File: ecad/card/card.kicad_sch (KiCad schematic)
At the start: 136 parts, among them J1 Conn_01x03_Pin, J2 USB4105-GF-A, J3 10145226-0241N13LF, J4 Conn_01x03_Pin, J5 Conn_01x03_Pin, SW1 SW_Push, SW2 SW_Push, U1 W25Q128JVS, U2 RP2350_80QFN, U3 MCP23017_SO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

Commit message: new panel routing
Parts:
- SW1, SW2: value SW_Push -> TS-1187A-B-A-B
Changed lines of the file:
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@@
 			)
 		)
-		(property "Value" "SW_Push"
+		(property "Value" "TS-1187A-B-A-B"
 			(at 30.48 94.742 0)
 			(effects
@@
 			)
 		)
-		(property "Value" "SW_Push"
+		(property "Value" "TS-1187A-B-A-B"
 			(at 32.512 205.74 0)
 			(effects

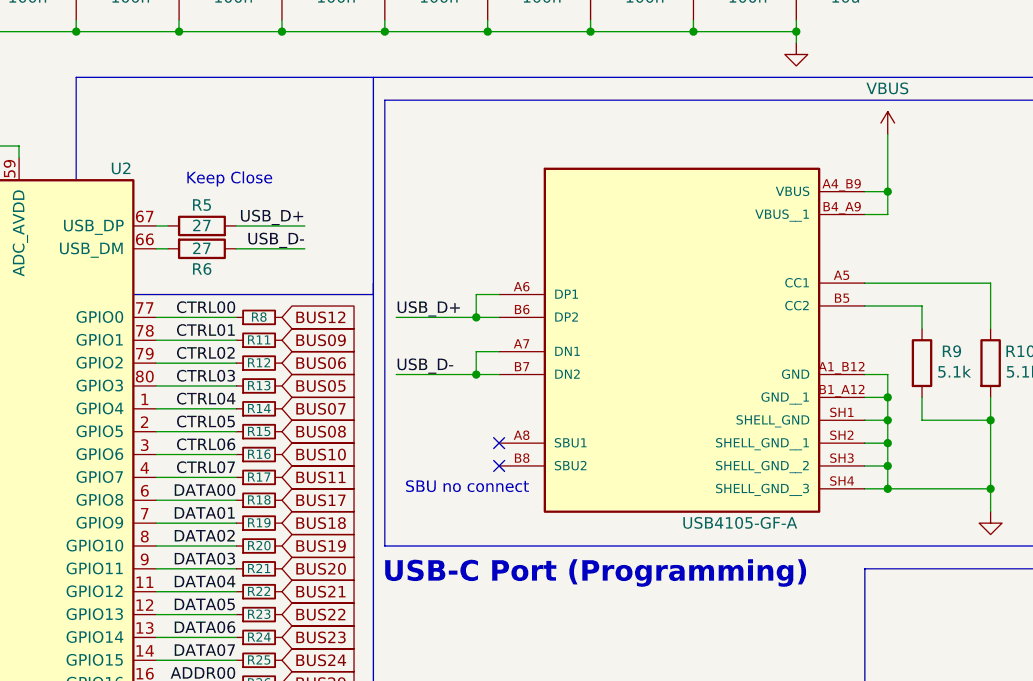
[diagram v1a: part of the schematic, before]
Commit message: stackup changes, prodction
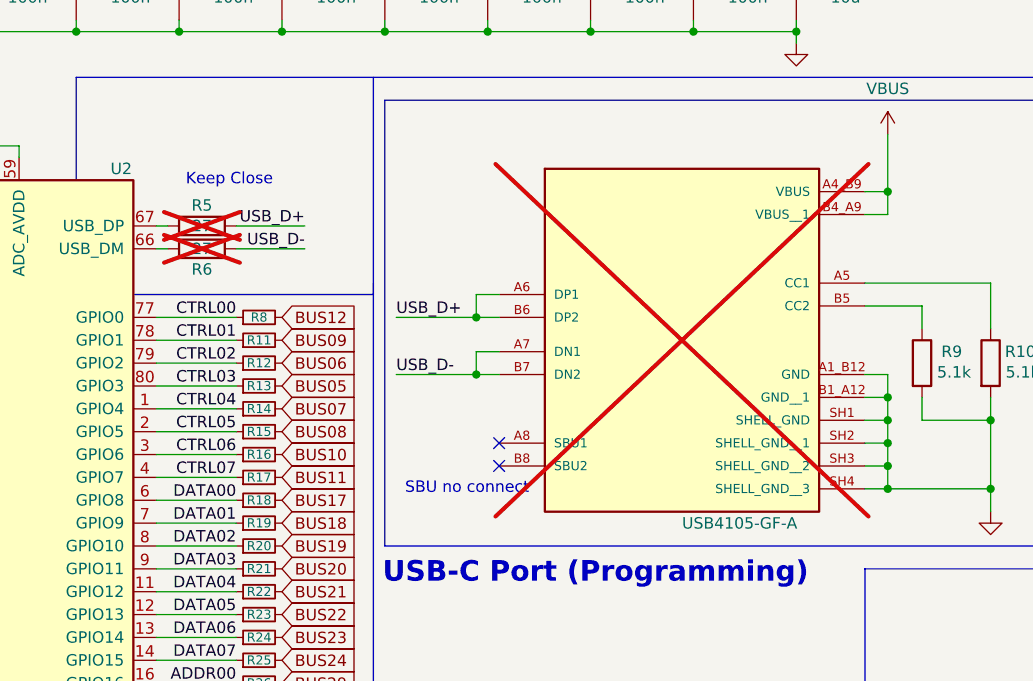
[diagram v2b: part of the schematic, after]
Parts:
- J2, R5, R6: now not fitted
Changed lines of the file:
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@@
 		(in_bom yes)
 		(on_board yes)
-		(dnp no)
+		(dnp yes)
 		(property "Reference" "J2"
 			(at 291.846 38.862 0)
@@
 		(in_bom yes)
 		(on_board yes)
-		(dnp no)
+		(dnp yes)
 		(property "Reference" "R6"
 			(at 146.05 64.516 90)
@@
 		(in_bom yes)
 		(on_board yes)
-		(dnp no)
+		(dnp yes)
 		(property "Reference" "R5"
 			(at 146.05 57.404 90)

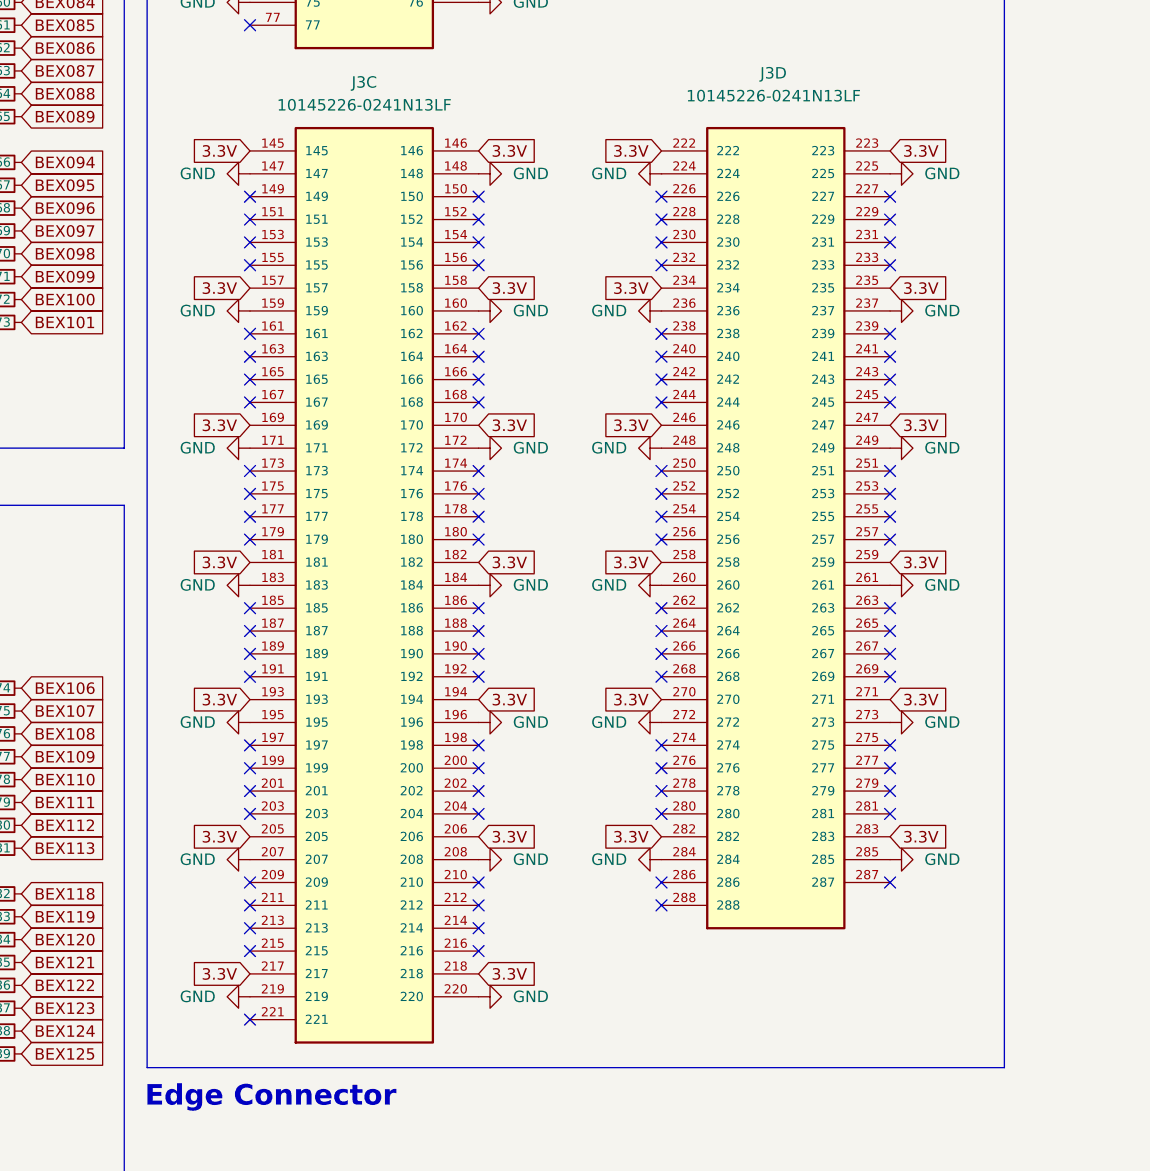
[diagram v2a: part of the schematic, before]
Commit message: double up for HASL
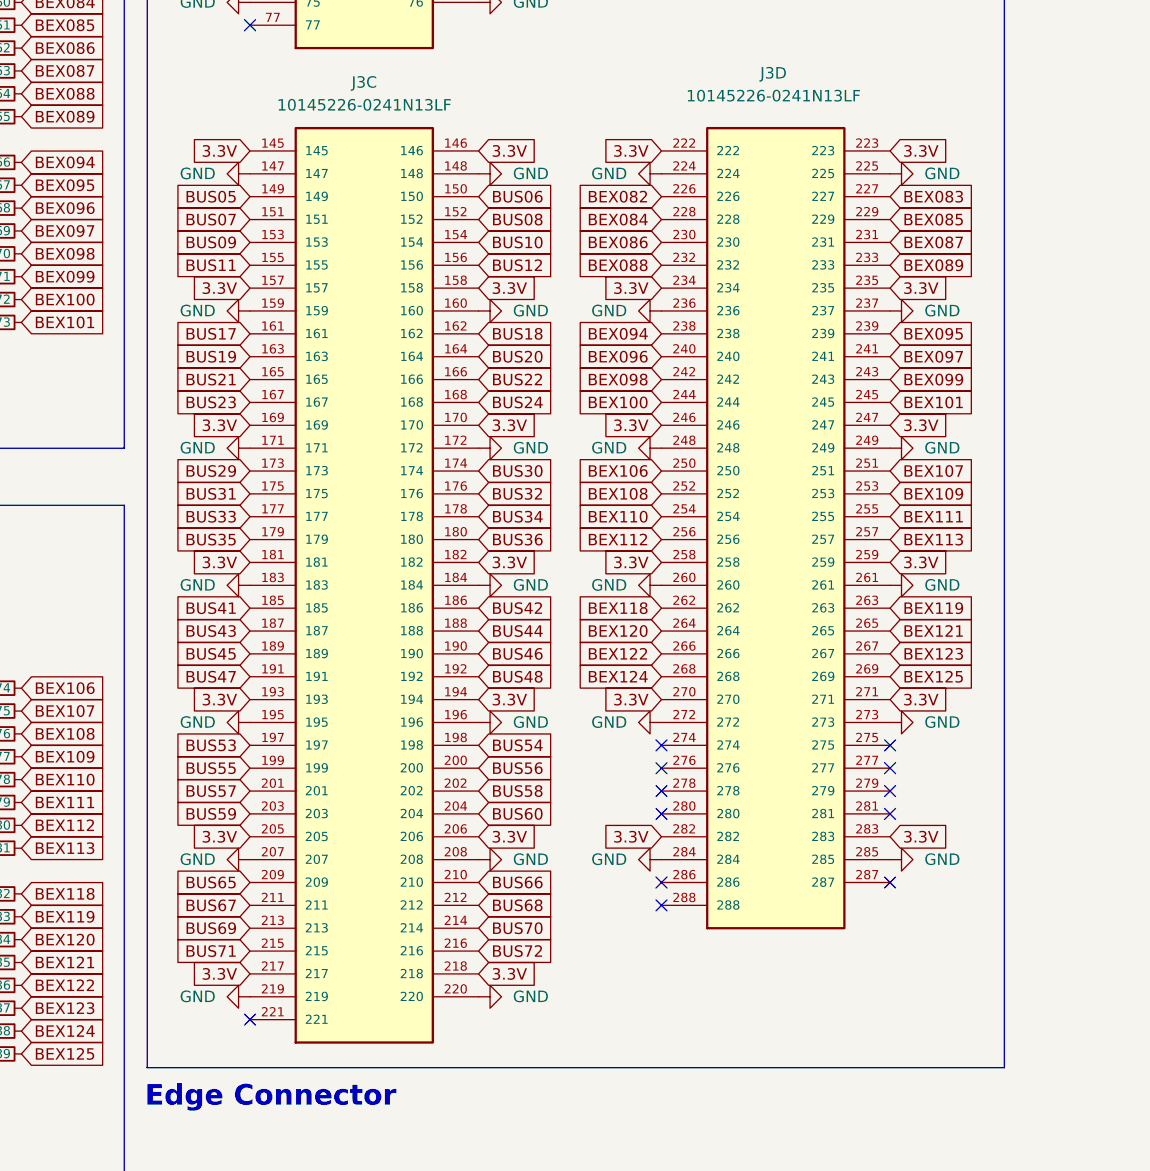
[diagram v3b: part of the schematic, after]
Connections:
- net BEX082: now also J3.226
- net BEX083: now also J3.227
- net BEX084: now also J3.228
- net BEX085: now also J3.229
- net BEX086: now also J3.230
- net BEX087: now also J3.231
- net BEX088: now also J3.232
- net BEX089: now also J3.233
- net BEX094: now also J3.238
- net BEX095: now also J3.239
- net BEX096: now also J3.240
- net BEX097: now also J3.241
- net BEX098: now also J3.242
- net BEX099: now also J3.243
- net BEX100: now also J3.244
- net BEX101: now also J3.245
- net BEX106: now also J3.250
- net BEX107: now also J3.251
- net BEX108: now also J3.252
- net BEX109: now also J3.253
- net BEX110: now also J3.254
- net BEX111: now also J3.255
- net BEX112: now also J3.256
- net BEX113: now also J3.257
- net BEX118: now also J3.262
- net BEX119: now also J3.263
- net BEX120: now also J3.264
- net BEX121: now also J3.265
- net BEX122: now also J3.266
- net BEX123: now also J3.267
- net BEX124: now also J3.268
- net BEX125: now also J3.269
- net BUS05: now also J3.149
- net BUS06: now also J3.150
- net BUS07: now also J3.151
- net BUS08: now also J3.152
- net BUS09: now also J3.153
- net BUS10: now also J3.154
- net BUS11: now also J3.155
- net BUS12: now also J3.156
- net BUS17: now also J3.161
- net BUS18: now also J3.162
- net BUS19: now also J3.163
- net BUS20: now also J3.164
- net BUS21: now also J3.165
- net BUS22: now also J3.166
- net BUS23: now also J3.167
- net BUS24: now also J3.168
- net BUS29: now also J3.173
- net BUS30: now also J3.174
- net BUS31: now also J3.175
- net BUS32: now also J3.176
- net BUS33: now also J3.177
- net BUS34: now also J3.178
- net BUS35: now also J3.179
- net BUS36: now also J3.180
- net BUS41: now also J3.185
- net BUS42: now also J3.186
- net BUS43: now also J3.187
- net BUS44: now also J3.188
- net BUS45: now also J3.189
- net BUS46: now also J3.190
- net BUS47: now also J3.191
- net BUS48: now also J3.192
- net BUS53: now also J3.197
- net BUS54: now also J3.198
- net BUS55: now also J3.199
- net BUS56: now also J3.200
- net BUS57: now also J3.201
- net BUS58: now also J3.202
- net BUS59: now also J3.203
- net BUS60: now also J3.204
- net BUS65: now also J3.209
- net BUS66: now also J3.210
- net BUS67: now also J3.211
- net BUS68: now also J3.212
- net BUS69: now also J3.213
- net BUS70: now also J3.214
- net BUS71: now also J3.215
- net BUS72: now also J3.216
- no-connect marks 110 -> 30

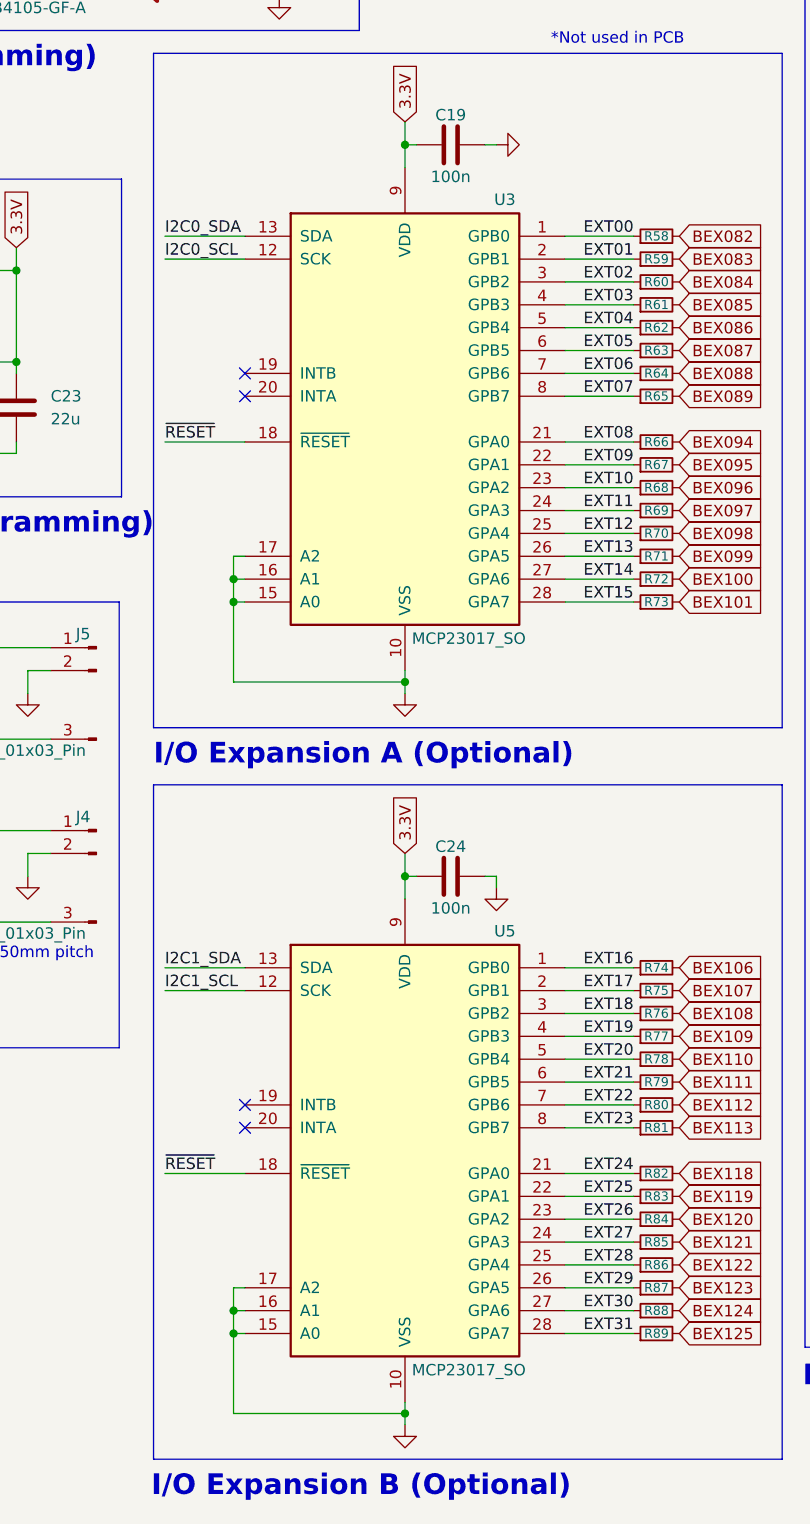
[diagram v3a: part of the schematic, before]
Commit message: fixup panel io expansion pinout
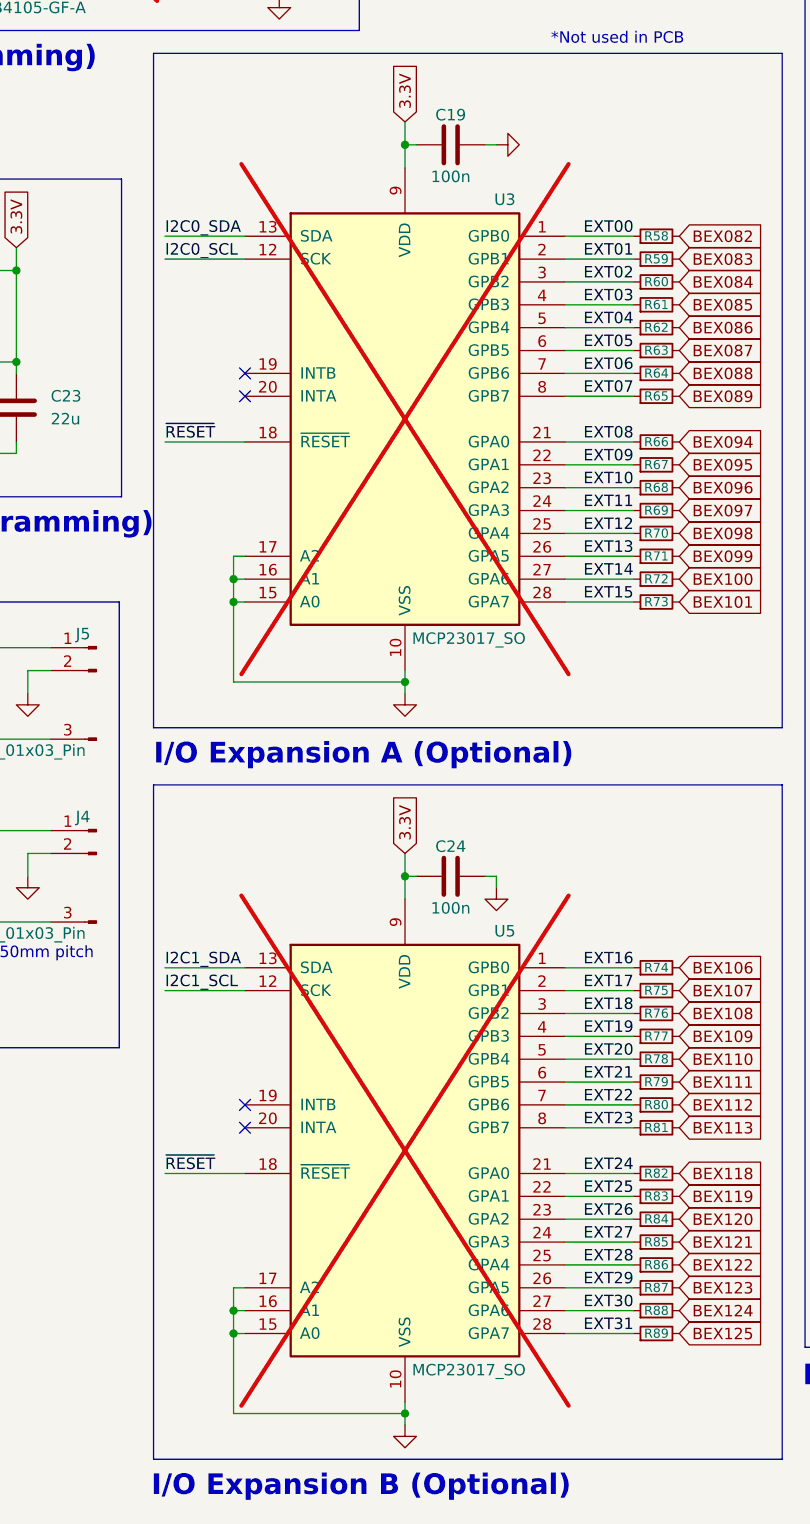
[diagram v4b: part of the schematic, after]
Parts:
- U3, U5: now not fitted
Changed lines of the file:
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@@
 		(in_bom yes)
 		(on_board yes)
-		(dnp no)
+		(dnp yes)
 		(property "Reference" "U3"
 			(at 257.556 114.046 0)
@@
 		(in_bom yes)
 		(on_board yes)
-		(dnp no)
+		(dnp yes)
 		(property "Reference" "U5"
 			(at 257.556 195.326 0)

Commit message: production fixups
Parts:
- L1: LCSC Part # (none) -> C42411119
- U2: value RP2350_80QFN -> RP2350B
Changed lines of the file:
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@@
 			)
 		)
-		(property "Value" "RP2350_80QFN"
+		(property "Value" "RP2350B"
 			(at 123.952 198.374 0)
 			(effects
@@
 			(effects
 				(font
+					(size 1.27 1.27)
+				)
+				(hide yes)
+			)
+		)
+		(property "LCSC Part #" "C42411119"
+			(at 59.69 68.58 90)
+			(effects
+				(font

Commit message: additional production fixups
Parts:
- J1, J4, J5: now not fitted
- J3: now left out of the parts list
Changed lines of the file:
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@@
 		(in_bom yes)
 		(on_board yes)
-		(dnp no)
+		(dnp yes)
 		(property "Reference" "J4"
 			(at 211.074 182.626 0)
@@
 		(in_bom yes)
 		(on_board yes)
-		(dnp no)
+		(dnp yes)
 		(property "Reference" "J1"
 			(at 55.626 190.246 0)
@@
 		(unit 4)
 		(exclude_from_sim no)
-		(in_bom yes)
+		(in_bom no)
 		(on_board yes)
 		(dnp no)
@@
 		(unit 1)
 		(exclude_from_sim no)
-		(in_bom yes)
+		(in_bom no)
 		(on_board yes)
 		(dnp no)
@@
 		(unit 2)
 		(exclude_from_sim no)
-		(in_bom yes)
+		(in_bom no)
 		(on_board yes)
 		(dnp no)
@@
 		(in_bom yes)
 		(on_board yes)
-		(dnp no)
+		(dnp yes)
 		(property "Reference" "J5"
 			(at 211.074 162.306 0)
@@
 		(unit 3)
 		(exclude_from_sim no)
-		(in_bom yes)
+		(in_bom no)
 		(on_board yes)
 		(dnp no)

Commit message: Files for JLCPCB
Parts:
- C21: footprint Capacitor_SMD:C_0402_1005Metric -> Capacitor_SMD:C_0805_2012Metric_Pad1.18x1.45mm_HandSolder; now not fitted
- C22, C23, D1, J3, U4: now not fitted
- R10, R9: footprint Resistor_SMD:R_0402_1005Metric -> Resistor_SMD:R_0603_1608Metric_Pad0.98x0.95mm_HandSolder; now not fitted
- R5, R6: footprint Capacitor_SMD:C_0603_1608Metric_Pad1.08x0.95mm_HandSolder -> Resistor_SMD:R_0603_1608Metric_Pad0.98x0.95mm_HandSolder
- R7: footprint Resistor_SMD:R_0402_1005Metric -> Resistor_SMD:R_0805_2012Metric_Pad1.20x1.40mm_HandSolder; now not fitted
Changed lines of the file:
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@@
 			)
 		)
-		(property "Footprint" "Capacitor_SMD:C_0603_1608Metric_Pad1.08x0.95mm_HandSolder"
+		(property "Footprint" "Resistor_SMD:R_0603_1608Metric_Pad0.98x0.95mm_HandSolder"
 			(at 146.05 60.452 90)
 			(effects
@@
 		(in_bom yes)
 		(on_board yes)
-		(dnp no)
+		(dnp yes)
 		(fields_autoplaced yes)
 		(property "Reference" "U4"
@@
 		(in_bom yes)
 		(on_board yes)
-		(dnp no)
+		(dnp yes)
 		(property "Reference" "R10"
 			(at 236.982 73.66 0)
@@
 			)
 		)
-		(property "Footprint" "Resistor_SMD:R_0402_1005Metric"
+		(property "Footprint" "Resistor_SMD:R_0603_1608Metric_Pad0.98x0.95mm_HandSolder"
 			(at 231.902 74.93 90)
 			(effects
@@
 		(in_bom yes)
 		(on_board yes)
-		(dnp no)
+		(dnp yes)
 		(fields_autoplaced yes)
 		(property "Reference" "C23"
@@
 		(in_bom yes)
 		(on_board yes)
-		(dnp no)
+		(dnp yes)
 		(property "Reference" "R7"
 			(at 28.194 191.77 0)
@@
 			)
 		)
-		(property "Footprint" "Resistor_SMD:R_0402_1005Metric"
+		(property "Footprint" "Resistor_SMD:R_0805_2012Metric_Pad1.20x1.40mm_HandSolder"
 			(at 32.258 191.77 90)
 			(effects
@@
 		(in_bom yes)
 		(on_board yes)
-		(dnp no)
+		(dnp yes)
 		(fields_autoplaced yes)
 		(property "Reference" "C22"
@@
 		(in_bom yes)
 		(on_board yes)
-		(dnp no)
+		(dnp yes)
 		(fields_autoplaced yes)
 		(property "Reference" "D1"
@@
 		(in_bom yes)
 		(on_board yes)
-		(dnp no)
+		(dnp yes)
 		(fields_autoplaced yes)
 		(property "Reference" "C21"
@@
 			)
 		)
-		(property "Footprint" "Capacitor_SMD:C_0402_1005Metric"
+		(property "Footprint" "Capacitor_SMD:C_0805_2012Metric_Pad1.18x1.45mm_HandSolder"
 			(at 213.0552 36.83 0)
 			(effects
@@
 		(in_bom yes)
 		(on_board yes)
-		(dnp no)
+		(dnp yes)
 		(property "Reference" "R9"
 			(at 229.362 73.66 0)
@@
 			)
 		)
-		(property "Footprint" "Resistor_SMD:R_0402_1005Metric"
+		(property "Footprint" "Resistor_SMD:R_0603_1608Metric_Pad0.98x0.95mm_HandSolder"
 			(at 224.282 74.93 90)
 			(effects
@@
 		(in_bom no)
 		(on_board yes)
-		(dnp no)
+		(dnp yes)
 		(property "Reference" "J3"
 			(at 361.696 131.064 0)
@@
 		(in_bom no)
 		(on_board yes)
-		(dnp no)
+		(dnp yes)
 		(fields_autoplaced yes)
 		(property "Reference" "J3"
@@
 			)
 		)
-		(property "Footprint" "Capacitor_SMD:C_0603_1608Metric_Pad1.08x0.95mm_HandSolder"
+		(property "Footprint" "Resistor_SMD:R_0603_1608Metric_Pad0.98x0.95mm_HandSolder"
 			(at 146.05 61.468 90)
 			(effects
@@
 		(in_bom no)
 		(on_board yes)
-		(dnp no)
+		(dnp yes)
 		(property "Reference" "J3"
 			(at 361.95 21.336 0)
@@
 		(in_bom no)
 		(on_board yes)
-		(dnp no)
+		(dnp yes)
 		(fields_autoplaced yes)
 		(property "Reference" "J3"
